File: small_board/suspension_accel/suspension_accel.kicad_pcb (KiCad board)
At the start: 2 copper layers, 20 x 76 mm, 19 parts, among them IC1 TJA1050T_CM,118, IC2 AMS1117-3.3, IC3 ESP32-S3-MINI-1-N8, IC4 LSM6DSV16BXTR, J1 OSTTE040104, J2 BM04B-GVHS-TB_LF__SN_

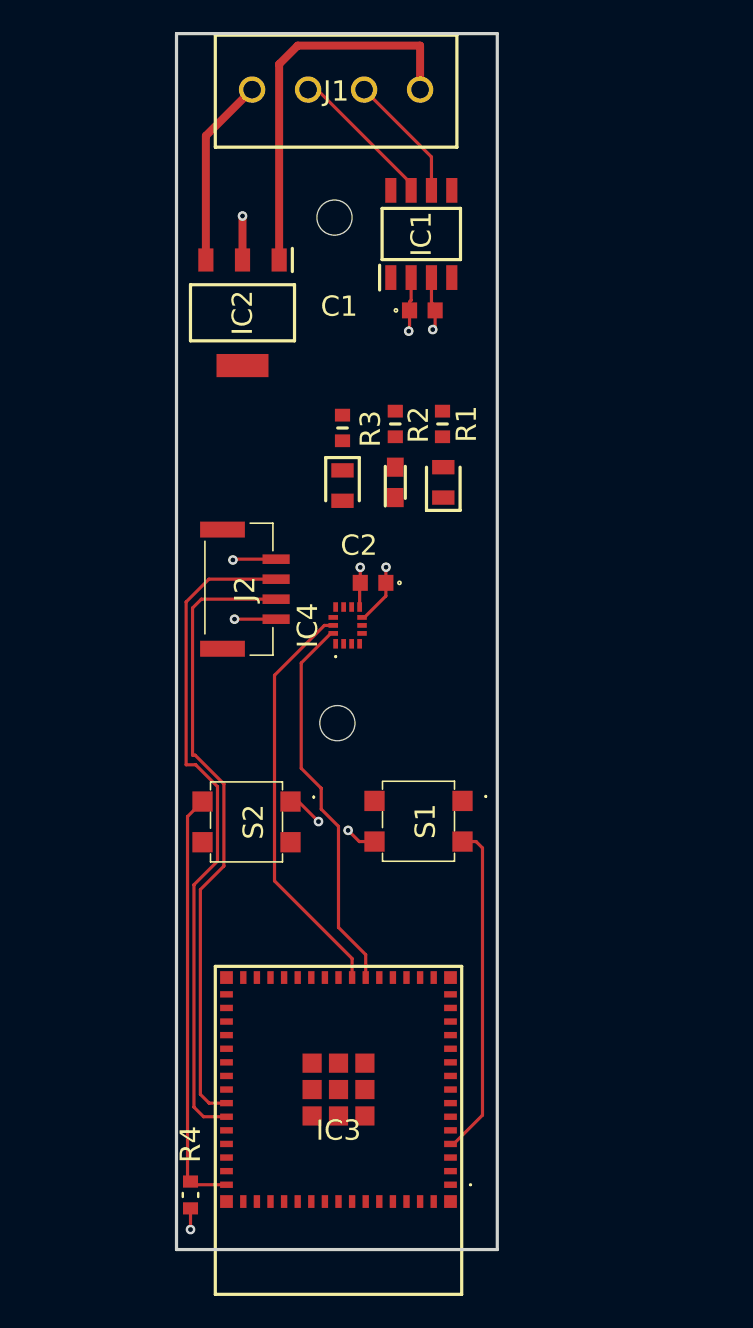
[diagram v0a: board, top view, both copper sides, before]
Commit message: added strain gauge adc, strain gauge ldo, comp components and headers for load cell hookups
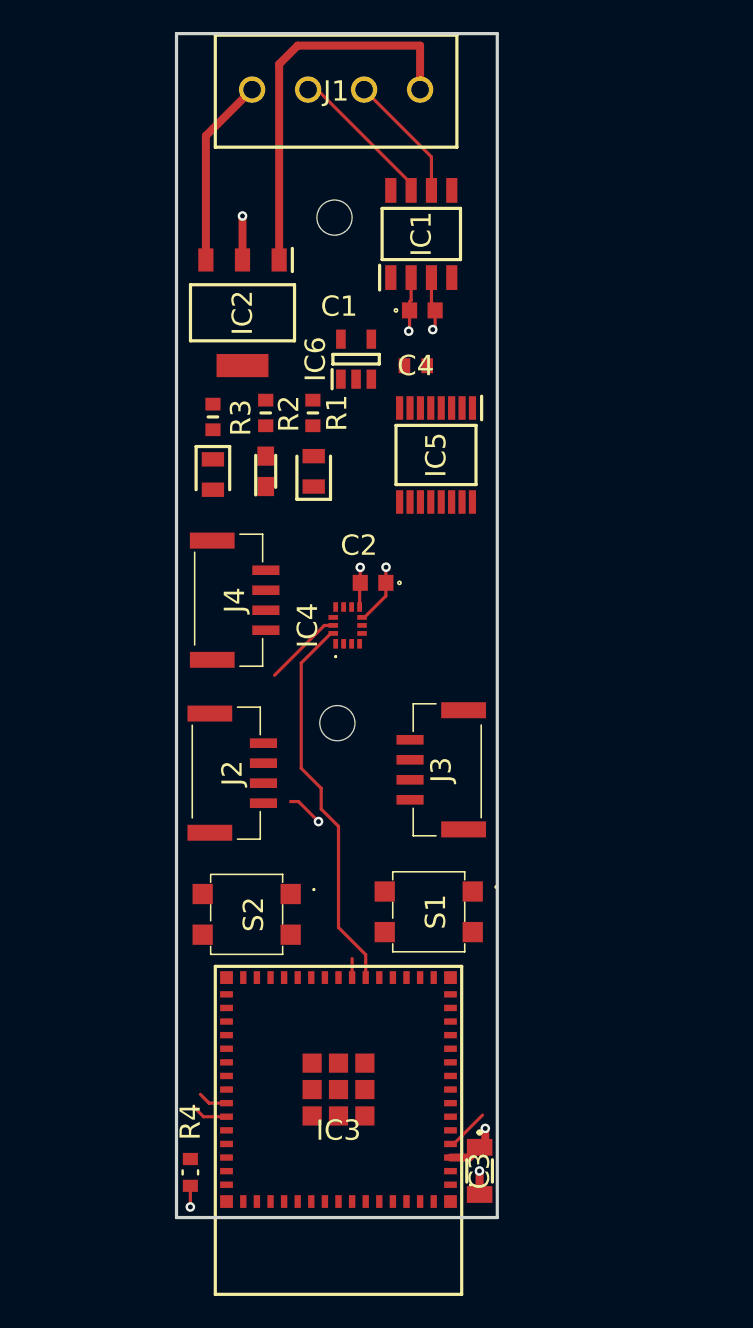
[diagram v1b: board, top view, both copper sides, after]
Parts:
- added C3: GRM31CR61A107MEA8L, Library:GRM31x, F.Cu at (41.3, 95.1)
- added C4: CL10A106KP8NNNC, Library:CAPC1608X90N, F.Cu at (37.3, 44.8)
- added IC5: ADS1220IPWR, Library:SOP65P640X120-16N, F.Cu at (38.6, 50.3)
- added IC6: TLV75533PDBVR, Library:SOT95P280X145-5N, F.Cu at (33.6, 44.4)
- added J3: BM04B-GVHS-TB_LF__SN_, Library:BM04BGVHSTBLFSN, F.Cu at (39.2, 70.0)
- added J4: BM04B-GVHS-TB_LF__SN_, Library:BM04BGVHSTBLFSN, F.Cu at (25.7, 59.4)
- moved J2 11.5 mm to (25.6, 70.2)
- moved BLINK_LED1 8.13 mm to (24.6, 51.6)
- moved R1 8.13 mm to (30.9, 47.7)
- moved R3 8.13 mm to (24.6, 48.0)
- moved CAN_LED1 8.13 mm to (27.9, 51.4)
- moved PWR_LED1 8.13 mm to (30.9, 51.4)
- moved R2 8.13 mm to (27.9, 47.7)
- moved S2 5.78 mm to (26.8, 79.0)
- moved S1 5.70 mm to (38.1, 78.9)
- moved R4 1.41 mm to (23.2, 95.2)
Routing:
- net Net-(IC3-RXD0): track 41.8 -> 2.28 mm
- net Net-(IC3-TXD0): track 39.2 -> 1.86 mm
- net Net-(IC3-EN): track 26.5 -> 0.55 mm
- net Net-(IC3-IO18): track 25.9 -> 6.15 mm
- net Net-(IC3-IO0): track 20.9 -> 2.75 mm
- net +3.3V: track 4.07 -> 7.49 mm, vias 2 -> 3
- net GND: track 38.7 -> 35.6 mm, vias 5 -> 4
- net +5V: track 18.2 -> 15.6 mm, vias 2 -> 1
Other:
- board size 20 x 76 mm -> 20 x 74 mm

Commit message: Added rev polarity protection, ads1220, routed, tja1050 level shifter, etc...
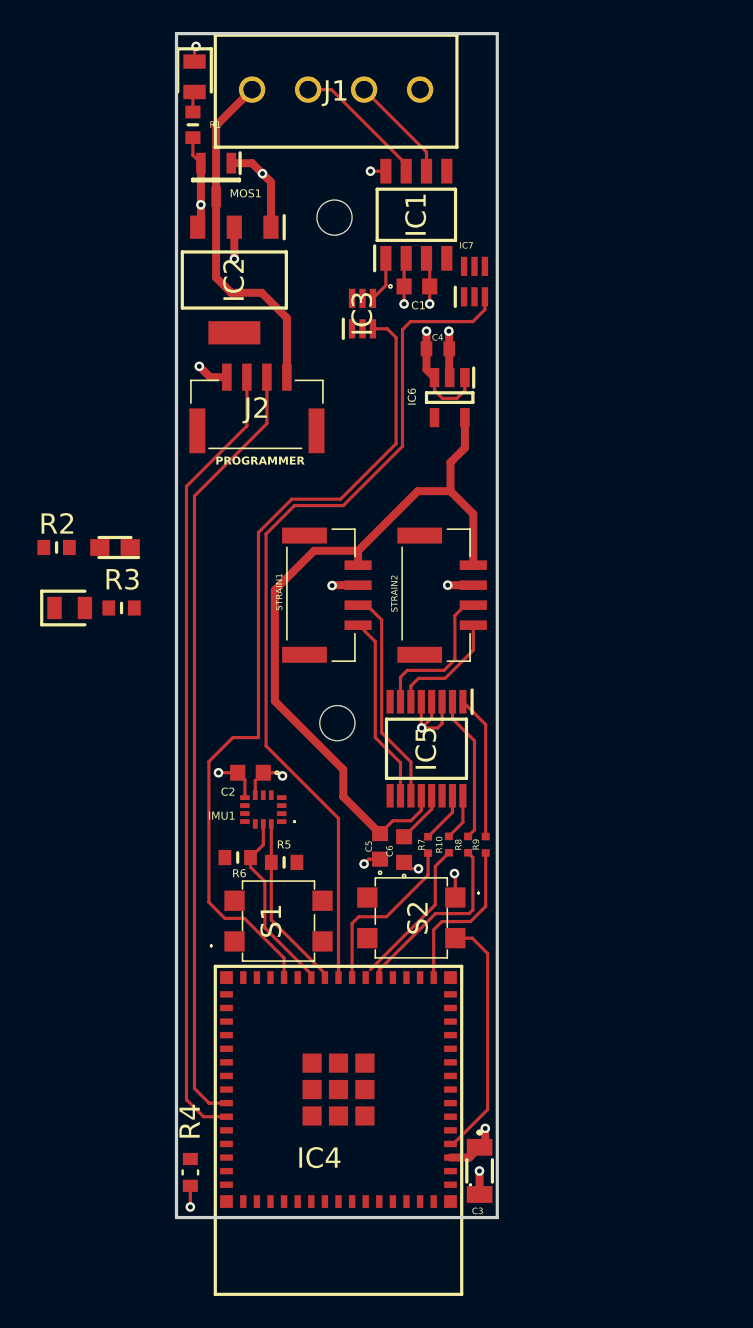
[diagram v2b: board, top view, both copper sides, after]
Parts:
- added C5: C0603C104K5RACTU, Library:C0603, F.Cu at (35.1, 74.8)
- added C6: C0603C104K5RACTU, Library:C0603, F.Cu at (36.6, 75.0)
- added IC3: SN74LVC1T45DCKR, Library:SOT65P210X110-6N, F.Cu at (34.0, 41.5)
- added IC7: SN74LVC1T45DCKR, Library:SOT65P210X110-6N, F.Cu at (41.0, 39.5)
- added MOS1: SI2301CDS-T1-GE3, Library:SOT95P237X112-3N, F.Cu at (24.9, 33.1)
- added R10: ERA2AEB470X, Library:ERA2AED122X, F.Cu at (39.4, 74.7)
- added R5: RC0603FR-073K3L, Library:RESC1608X55N, F.Cu at (29.1, 75.8)
- added R6: RC0603FR-073K3L, Library:RESC1608X55N, F.Cu at (26.2, 75.5)
- added R7: ERA2AEB470X, Library:ERA2AED122X, F.Cu at (38.1, 74.7)
- added R8: ERA2AEB470X, Library:ERA2AED122X, F.Cu at (40.6, 74.7)
- added R9: ERA2AEB470X, Library:ERA2AED122X, F.Cu at (41.7, 74.7)
- moved PWR_LED1 25.8 mm to (23.5, 26.7), turned to -90 degrees
- moved J2 22.6 mm to (27.4, 47.7), turned to 0 degrees
- moved R1 19.5 mm to (23.4, 29.7), turned to -90 degrees
- moved IC5 18.4 mm to (38.0, 68.7)
- moved R2 15.5 mm to (14.9, 56.1), turned to 180 degrees
- moved C2 14.1 mm to (27.0, 70.2)
- moved STRAIN1 13.4 mm to (31.5, 59.1), turned to -90 degrees
- moved R3 13.2 mm to (18.9, 59.9), turned to 0 degrees
- moved STRAIN2 13.0 mm to (38.7, 59.1)
- moved IMU1 12.7 mm to (27.8, 72.5), turned to 180 degrees
- moved BLINK_LED1 12.2 mm to (15.7, 59.9), turned to 0 degrees
- moved CAN_LED1 10.6 mm to (18.5, 56.1), turned to 180 degrees
- moved S2 10.3 mm to (37.0, 79.3)
- moved S1 9.41 mm to (28.8, 79.5), turned to 90 degrees
- moved IC6 6.32 mm to (39.5, 46.8), turned to -90 degrees
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- renumbered IC3 to IC4, IC4 to IMU1, J3 to STRAIN1, J4 to STRAIN2
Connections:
- C2 pad 2: Net-(IC4-VDD) -> +3.3V
- IC1 pad 1: unconnected-(IC1-TXD-Pad1) -> Net-(IC1-TXD)
- IC1 pad 4: unconnected-(IC1-RXD-Pad4) -> Net-(IC1-RXD)
- IC1 pad 8: unconnected-(IC1-S-Pad8) -> GND
- IC4 pad 1: unconnected-(IC3-GND_1-Pad1) -> GND
- IC4 pad 16: unconnected-(IC3-IO12-Pad16) -> Net-(IC4-IO12)
- IC4 pad 2: unconnected-(IC3-GND_2-Pad2) -> GND
- IC4 pad 20: unconnected-(IC3-IO16-Pad20) -> Net-(IC4-IO16)
- IC4 pad 21: Net-(IC3-IO17) -> Net-(IC4-IO17)
- IC4 pad 22: Net-(IC3-IO18) -> /EXC+
- IC4 pad 23: unconnected-(IC3-IO19-Pad23) -> Net-(IC4-IO19)
- IC4 pad 24: unconnected-(IC3-IO20-Pad24) -> Net-(IC4-IO20)
- IC4 pad 25: unconnected-(IC3-IO21-Pad25) -> Net-(IC4-IO21)
- IC4 pad 27: unconnected-(IC3-IO47-Pad27) -> Net-(IC3-A)
- IC4 pad 4: Net-(IC3-IO0) -> Net-(IC4-IO0)
- IC4 pad 42: unconnected-(IC3-GND_3-Pad42) -> GND
- IC4 pad 43: unconnected-(IC3-GND_4-Pad43) -> GND
- IC4 pad 45: Net-(IC3-EN) -> Net-(IC4-EN)
- IC4 pad 46: unconnected-(IC3-GND_5-Pad46) -> GND
- IC4 pad 47: unconnected-(IC3-GND_6-Pad47) -> GND
- IC4 pad 48: unconnected-(IC3-GND_7-Pad48) -> GND
- IC4 pad 49: unconnected-(IC3-GND_8-Pad49) -> GND
- IC4 pad 50: unconnected-(IC3-GND_9-Pad50) -> GND
- IC4 pad 51: unconnected-(IC3-GND_10-Pad51) -> GND
- IC4 pad 52: unconnected-(IC3-GND_11-Pad52) -> GND
- IC4 pad 53: unconnected-(IC3-GND_12-Pad53) -> GND
- IC4 pad 54: unconnected-(IC3-GND_13-Pad54) -> GND
- IC4 pad 55: unconnected-(IC3-GND_14-Pad55) -> GND
- IC4 pad 56: unconnected-(IC3-GND_15-Pad56) -> GND
- IC4 pad 57: unconnected-(IC3-GND_16-Pad57) -> GND
- IC4 pad 58: unconnected-(IC3-GND_17-Pad58) -> GND
- IC4 pad 59: unconnected-(IC3-GND_18-Pad59) -> GND
- IC4 pad 60: unconnected-(IC3-GND_19-Pad60) -> GND
- IC4 pad 61: unconnected-(IC3-GND_20-Pad61) -> GND
- IC4 pad 62: unconnected-(IC3-GND_21-Pad62) -> GND
- IC4 pad 63: unconnected-(IC3-GND_22-Pad63) -> GND
- IC4 pad 64: unconnected-(IC3-GND_23-Pad64) -> GND
- IC4 pad 65: unconnected-(IC3-GND_24-Pad65) -> GND
- IC4 pad 66: unconnected-(IC3-GND_25-Pad66) -> GND
- IC4 pad 67: unconnected-(IC3-GND_26-Pad67) -> GND
- IC4 pad 68: unconnected-(IC3-GND_27-Pad68) -> GND
- IC4 pad 69: unconnected-(IC3-GND_28-Pad69) -> GND
- IC4 pad 70: unconnected-(IC3-GND_29-Pad70) -> GND
- IC4 pad 71: unconnected-(IC3-GND_30-Pad71) -> GND
- IC4 pad 72: unconnected-(IC3-GND_31-Pad72) -> GND
- IC4 pad 73: unconnected-(IC3-GND_32-Pad73) -> GND
- IC5 pad 1: unconnected-(IC5-SCLK-Pad1) -> Net-(IC5-SCLK)
- IC5 pad 10: unconnected-(IC5-AIN1-Pad10) -> /SIG-
- IC5 pad 11: unconnected-(IC5-AIN0/REFP1-Pad11) -> /SIG+
- IC5 pad 12: unconnected-(IC5-AVDD-Pad12) -> /EXC+
- IC5 pad 13: unconnected-(IC5-DVDD-Pad13) -> +3.3V
- IC5 pad 15: unconnected-(IC5-DOUT/~{DRDY}-Pad15) -> Net-(IC5-DOUT/~{DRDY})
- IC5 pad 16: unconnected-(IC5-DIN-Pad16) -> Net-(IC5-DIN)
- IC5 pad 2: unconnected-(IC5-~{CS}-Pad2) -> Net-(IC5-~{CS})
- IC5 pad 3: unconnected-(IC5-CLK-Pad3) -> GND
- IC5 pad 4: unconnected-(IC5-DGND-Pad4) -> GND
- IC5 pad 5: unconnected-(IC5-AVSS-Pad5) -> GND
- IC5 pad 6: unconnected-(IC5-AIN3/REFN1-Pad6) -> Net-(IC5-AIN3/REFN1)
- IC5 pad 7: unconnected-(IC5-AIN2-Pad7) -> Net-(IC5-AIN2)
- IC6 pad 5: unconnected-(IC6-OUT-Pad5) -> /EXC+
- IMU1 pad 13: Net-(IC3-IO18) -> Net-(IC4-IO21)
- IMU1 pad 14: Net-(IC3-IO17) -> Net-(IC4-IO20)
- IMU1 pad 8: Net-(IC4-VDD) -> +3.3V
- J1 pad 1: +5V -> Net-(MOS1-D)
- J2 pad 4: +5V -> Net-(MOS1-D)
- PWR_LED1 pad 2: Net-(PWR_LED1-A) -> unconnected-(PWR_LED1-A-Pad2)
- R1 pad 1: Net-(PWR_LED1-A) -> unconnected-(R1-Pad1)
- R4 pad 1: Net-(IC3-EN) -> Net-(IC4-EN)
- S1 pad A1: unconnected-(S1-COM_1-PadA1) -> Net-(IC4-EN)
- S1 pad A2: Net-(IC3-IO0) -> unconnected-(S1-NO_1-PadA2)
- S1 pad B1: unconnected-(S1-COM_2-PadB1) -> GND
- S1 pad B2: GND -> unconnected-(S1-NO_2-PadB2)
- S2 pad A2: unconnected-(S2-NO_1-PadA2) -> Net-(IC4-IO0)
- S2 pad B1: Net-(IC3-EN) -> unconnected-(S2-COM_2-PadB1)
- STRAIN1 pad 1: unconnected-(J3-Pad1) -> /EXC+
- STRAIN1 pad 2: unconnected-(J3-Pad2) -> GND
- STRAIN1 pad 3: unconnected-(J3-Pad3) -> /SIG+
- STRAIN1 pad 4: unconnected-(J3-Pad4) -> /SIG-
- STRAIN2 pad 1: unconnected-(J4-Pad1) -> /EXC+
- STRAIN2 pad 2: unconnected-(J4-Pad2) -> GND
- STRAIN2 pad 3: unconnected-(J4-Pad3) -> Net-(IC5-AIN2)
- STRAIN2 pad 4: unconnected-(J4-Pad4) -> Net-(IC5-AIN3/REFN1)
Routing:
- net /EXC+: track 0.00 -> 57.4 mm
- net Net-(IC4-IO19): track 0.00 -> 54.2 mm
- net Net-(IC3-A): track 0.00 -> 51.9 mm
- net Net-(IC4-RXD0): track 2.28 -> 49.7 mm
- net Net-(IC4-TXD0): track 1.86 -> 48.7 mm
- net Net-(IC3-IO17): track 24.1 -> 0.00 mm
- net Net-(MOS1-D): track 0.00 -> 21.9 mm
- net Net-(IC4-IO0): track 0.00 -> 15.6 mm
- net /SIG+: track 0.00 -> 13.6 mm
- net /SIG-: track 0.00 -> 11.8 mm
- net Net-(IC4-IO16): track 0.00 -> 11.6 mm
- net Net-(IC4-IO21): track 0.00 -> 11.5 mm
- net Net-(IC4-IO20): track 0.00 -> 11.0 mm
- net Net-(IC4-IO12): track 0.00 -> 10.2 mm
- net Net-(IC5-AIN2): track 0.00 -> 9.56 mm
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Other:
- board text added: "PROGRAMMER"

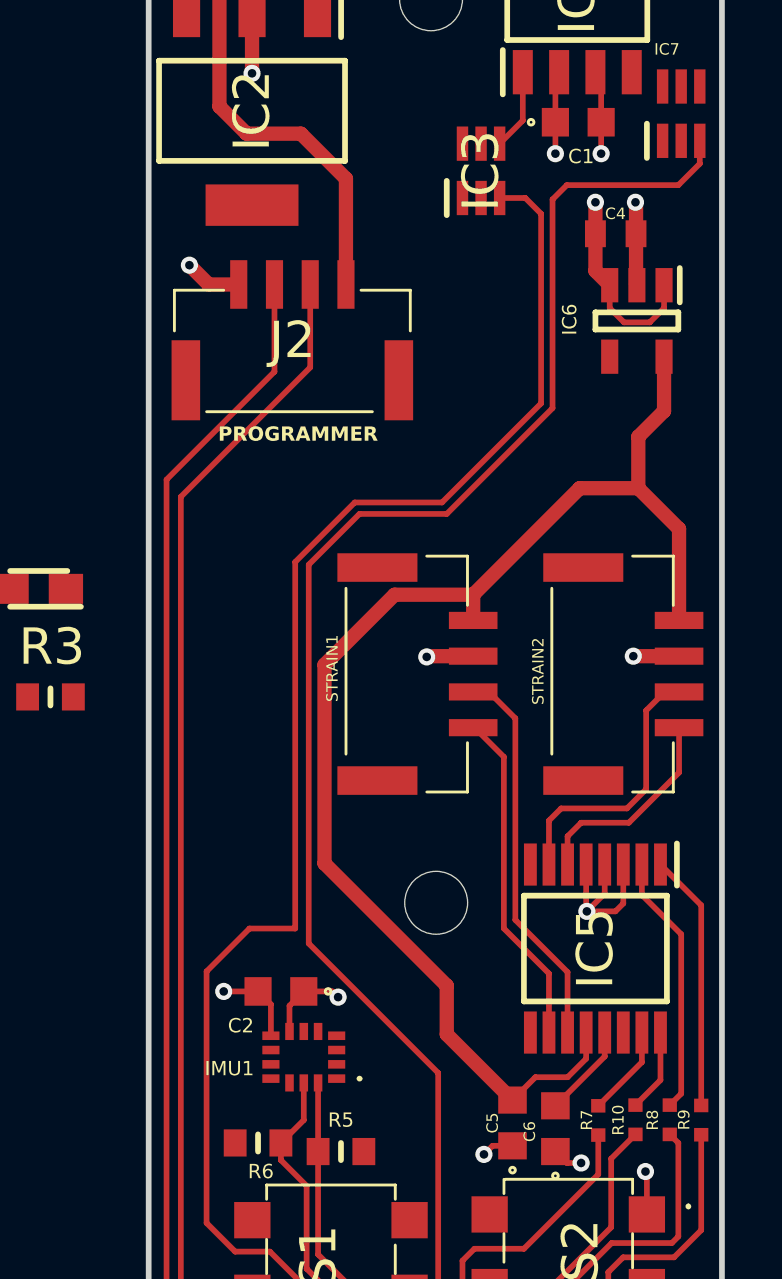
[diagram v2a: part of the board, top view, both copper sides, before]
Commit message: moved adc to provide space for filters
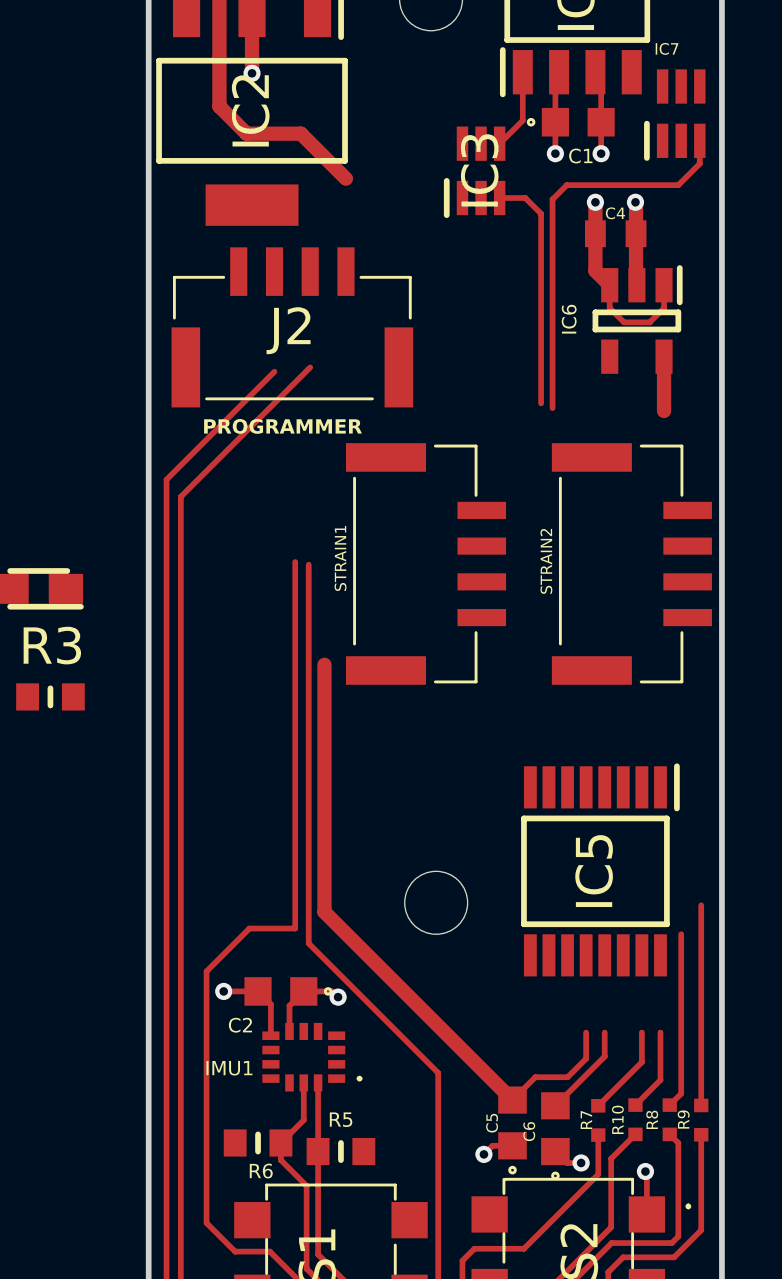
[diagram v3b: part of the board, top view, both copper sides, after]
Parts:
- moved STRAIN1 3.86 mm to (31.8, 55.2)
- moved STRAIN2 3.86 mm to (39.0, 55.2)
- moved IC5 2.70 mm to (38.0, 66.0)
- moved J2 0.45 mm to (27.4, 47.2)
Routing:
- net /EXC+: track 57.4 -> 34.7 mm
- net /SIG+: track 13.6 -> 0.00 mm
- net /SIG-: track 11.8 -> 0.00 mm
- net GND: track 33.2 -> 21.8 mm, vias 14 -> 10
- net Net-(IC3-A): track 51.9 -> 41.0 mm
- net Net-(IC4-IO19): track 54.2 -> 43.4 mm
- net Net-(IC5-AIN2): track 9.56 -> 0.00 mm
- net Net-(IC5-AIN3/REFN1): track 7.38 -> 0.00 mm
- net Net-(MOS1-D): track 21.9 -> 18.2 mm
- net Net-(IC4-RXD0): track 49.7 -> 46.6 mm
- net Net-(IC5-~{CS}): track 9.15 -> 6.14 mm
- net Net-(IC4-TXD0): track 48.7 -> 45.8 mm
- net Net-(IC5-SCLK): track 9.02 -> 7.00 mm

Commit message: not much changed
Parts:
- moved BLINK_LED1 15.3 mm to (30.0, 65.3), turned to 90 degrees
- moved R2 15.2 mm to (26.2, 66.2), turned to -90 degrees
- moved R3 11.3 mm to (30.0, 62.1), turned to 90 degrees
- moved CAN_LED1 10.0 mm to (26.2, 62.5), turned to -90 degrees
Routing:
- net Net-(IC5-DOUT/~{DRDY}): track 3.19 -> 0.00 mm
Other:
- copper layers 2 -> 4

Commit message: finished filter work, rerounted connection, bus level shifters connected, blink led connected, etc...
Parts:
- removed CAN_LED1: 150080GS75000, Library:LEDM2012X70N
- removed R2: RC0603FR-07220RL, Library:RESC1608X55N
- added C7: C0603C103F3GECTU, Library:CAPC1608X87N, F.Cu at (36.5, 60.8)
- added C8: C0603C103F3GECTU, Library:CAPC1608X87N, F.Cu at (36.2, 71.0)
- added R11: ERA-2AEB101X, Library:ERA2AED122X, F.Cu at (38.8, 60.0)
- added R12: ERA-2AEB101X, Library:ERA2AED122X, F.Cu at (36.8, 59.2)
- added R13: ERA-2AEB101X, Library:ERA2AED122X, F.Cu at (35.8, 72.2)
- added R14: ERA-2AEB101X, Library:ERA2AED122X, F.Cu at (34.5, 70.2)
- moved BLINK_LED1 12.2 mm to (27.0, 53.5), turned to -90 degrees
- moved R3 6.65 mm to (25.8, 57.0), turned to -90 degrees
- moved STRAIN2 1.60 mm to (38.0, 54.0)
- moved IC5 0.56 mm to (37.8, 65.5)
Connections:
- IC4 pad 10: Net-(IC4-IO6) -> unconnected-(IC4-IO6-Pad10)
- IC4 pad 38: unconnected-(IC4-IO42-Pad38) -> Net-(IC4-IO42)
- IC4 pad 9: Net-(IC4-IO5) -> unconnected-(IC4-IO5-Pad9)
- IC5 pad 10: /SIG- -> Net-(IC5-AIN1)
- IC5 pad 11: /SIG+ -> Net-(IC5-AIN0/REFP1)
- PWR_LED1 pad 2: unconnected-(PWR_LED1-A-Pad2) -> Net-(PWR_LED1-A)
- R1 pad 1: unconnected-(R1-Pad1) -> Net-(PWR_LED1-A)
- R3 pad 2: Net-(IC4-IO5) -> Net-(IC4-IO42)
- STRAIN1 pad 3: /SIG+ -> unconnected-(STRAIN1-Pad3)
- STRAIN1 pad 4: /SIG- -> Net-(R13-Pad2)
- STRAIN2 pad 3: Net-(IC5-AIN2) -> Net-(R12-Pad2)
- STRAIN2 pad 4: Net-(IC5-AIN3/REFN1) -> Net-(R11-Pad2)
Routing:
- net Net-(IC4-IO42): track 0.00 -> 33.8 mm
- net /EXC+: track 34.7 -> 55.1 mm
- net GND: track 21.8 -> 40.1 mm, vias 10 -> 14
- net Net-(R13-Pad2): track 0.00 -> 16.4 mm
- net (no net): track 1.29 -> 15.0 mm
- net Net-(IC3-A): track 41.0 -> 50.1 mm
- net Net-(IC4-IO19): track 43.4 -> 52.4 mm
- net +3.3V: track 12.9 -> 20.1 mm, vias 4 -> 5
- net Net-(R12-Pad2): track 0.00 -> 6.55 mm
- net Net-(IC5-~{CS}): track 6.14 -> 12.5 mm
- net Net-(IC5-DOUT/~{DRDY}): track 0.00 -> 6.29 mm
- net Net-(IC5-SCLK): track 7.00 -> 12.3 mm
- net +5V: track 15.8 -> 20.6 mm, vias 3 -> 4
- net Net-(IC5-AIN0/REFP1): track 0.00 -> 4.31 mm
- net Net-(R11-Pad2): track 0.00 -> 4.22 mm
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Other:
- board text added: "BLINK LED"
